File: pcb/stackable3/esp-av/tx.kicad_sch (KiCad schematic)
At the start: 35 parts, among them J6 PJ-327U, J7 PJ-327U, J8 PJ-327U, J9 PJ-327U, Q1 PDNM6ET20V05, Q10 DMP1045U, Q11 DMP1045U, Q12 DMP1045U, Q13 DMP1045U, Q3 DMP1045U, Q4 DMP1045U, Q5 DMP1045U, Q6 DMP1045U

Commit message: Replace discrete resistor footprints with built-ins on stackable3 boards
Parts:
- R18, R19, R20, R22: footprint discrete:R_0603_1608Metric -> Resistor_SMD:R_0603_1608Metric
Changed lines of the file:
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@@
 			)
 		)
-		(property "Footprint" "discrete:R_0603_1608Metric"
+		(property "Footprint" "Resistor_SMD:R_0603_1608Metric"
 			(at 245.11 121.158 90)
 			(effects
@@
 			)
 		)
-		(property "Footprint" "discrete:R_0603_1608Metric"
+		(property "Footprint" "Resistor_SMD:R_0603_1608Metric"
 			(at 245.11 89.408 90)
 			(effects
@@
 			)
 		)
-		(property "Footprint" "discrete:R_0603_1608Metric"
+		(property "Footprint" "Resistor_SMD:R_0603_1608Metric"
 			(at 245.11 152.908 90)
 			(effects
@@
 			)
 		)
-		(property "Footprint" "discrete:R_0603_1608Metric"
+		(property "Footprint" "Resistor_SMD:R_0603_1608Metric"
 			(at 245.11 56.388 90)
 			(effects

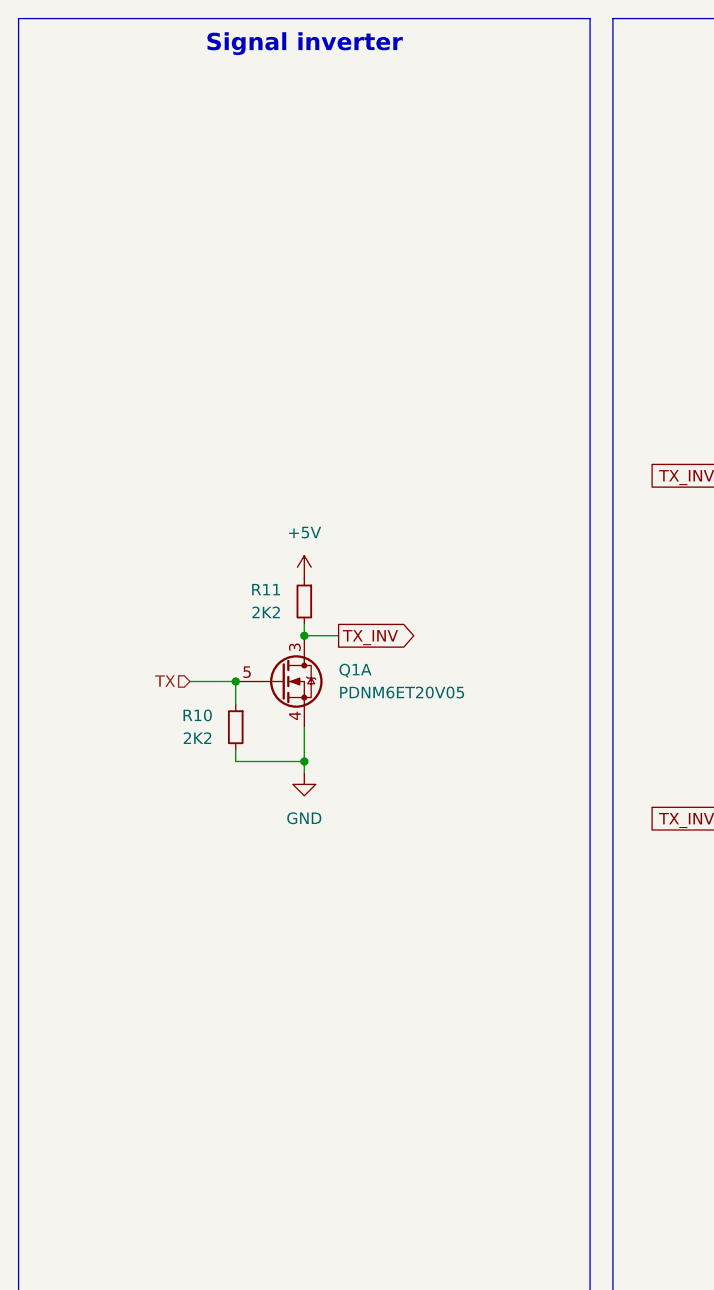
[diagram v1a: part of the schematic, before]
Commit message: Update stackable3/esp-av IR repeater control circuit
This replaces the N-channel repeater signal control MOSFET with a
P-channel MOSFET (driven by an N-channel MOSFET at -5V)
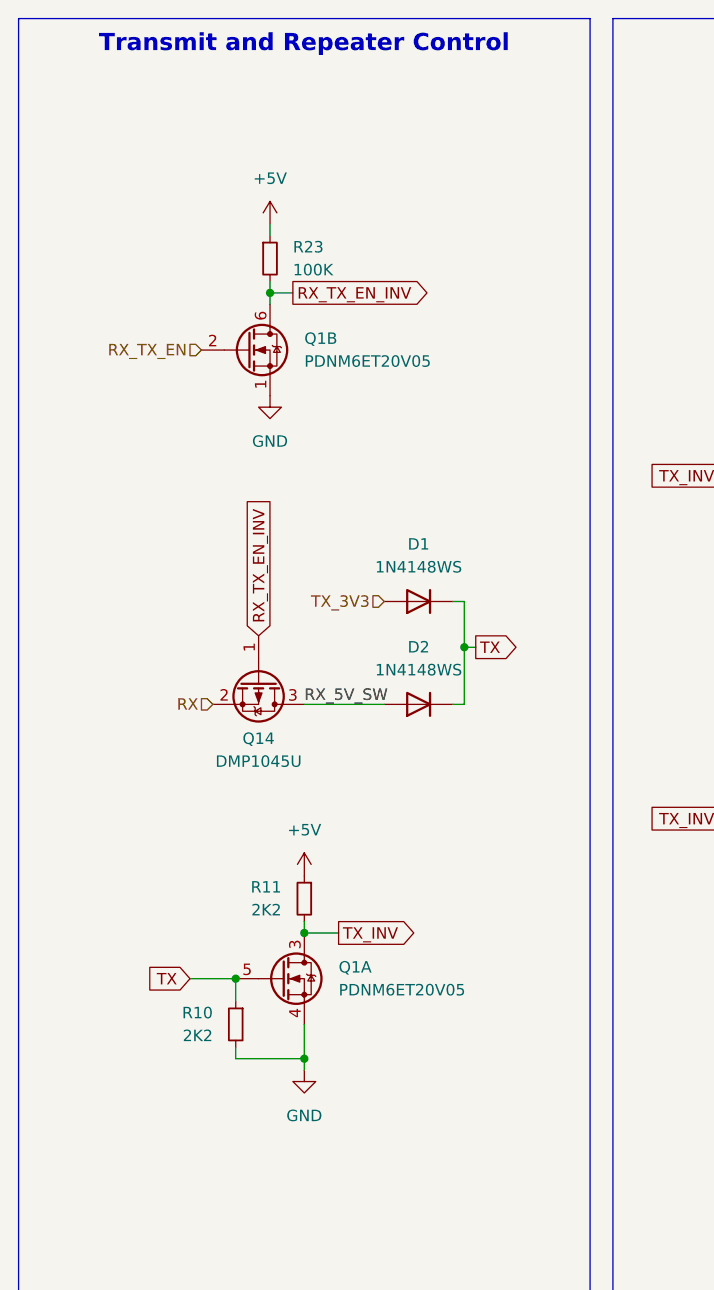
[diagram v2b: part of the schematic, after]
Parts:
- added D1, D2: 1N4148WS, package:D_SOD-323, symbol Diode:1N4148WS
- added unit 2 of Q1
- added Q14: DMP1045U, Package_TO_SOT_SMD:SOT-23, symbol discrete:DMP1045U
- added R23: 100K, Resistor_SMD:R_0603_1608Metric, symbol Device:R_Small
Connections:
- net +5V: now also R23.1
- net GND: now also Q1.1 (S)
- net TX: now also D1.1 (K), D2.1 (K)
- new net RX: Q14.2 (S)
- new net RX_5V_SW: D2.2 (A), Q14.3 (D)
- new net RX_TX_EN: Q1.2 (G)
- new net RX_TX_EN_INV: Q1.6 (D), Q14.1 (G), R23.2
- new net TX_3V3: D1.2 (A)
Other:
- moved on the sheet: Q1A, R10, R11

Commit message: Rename mode LEDs GND net on stackable3/esp-av
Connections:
- net DEBUG_LED_GND renamed MODE_LED_GND
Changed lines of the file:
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@@
 		)
 	)
-	(global_label "DEBUG_LED_GND"
+	(global_label "MODE_LED_GND"
 		(shape output)
 		(at 256.54 54.61 0)
@@
 		)
 	)
-	(global_label "DEBUG_LED_GND"
+	(global_label "MODE_LED_GND"
 		(shape output)
 		(at 256.54 87.63 0)
@@
 		)
 	)
-	(global_label "DEBUG_LED_GND"
+	(global_label "MODE_LED_GND"
 		(shape output)
 		(at 256.54 151.13 0)
@@
 		)
 	)
-	(global_label "DEBUG_LED_GND"
+	(global_label "MODE_LED_GND"
 		(shape output)
 		(at 256.54 119.38 0)

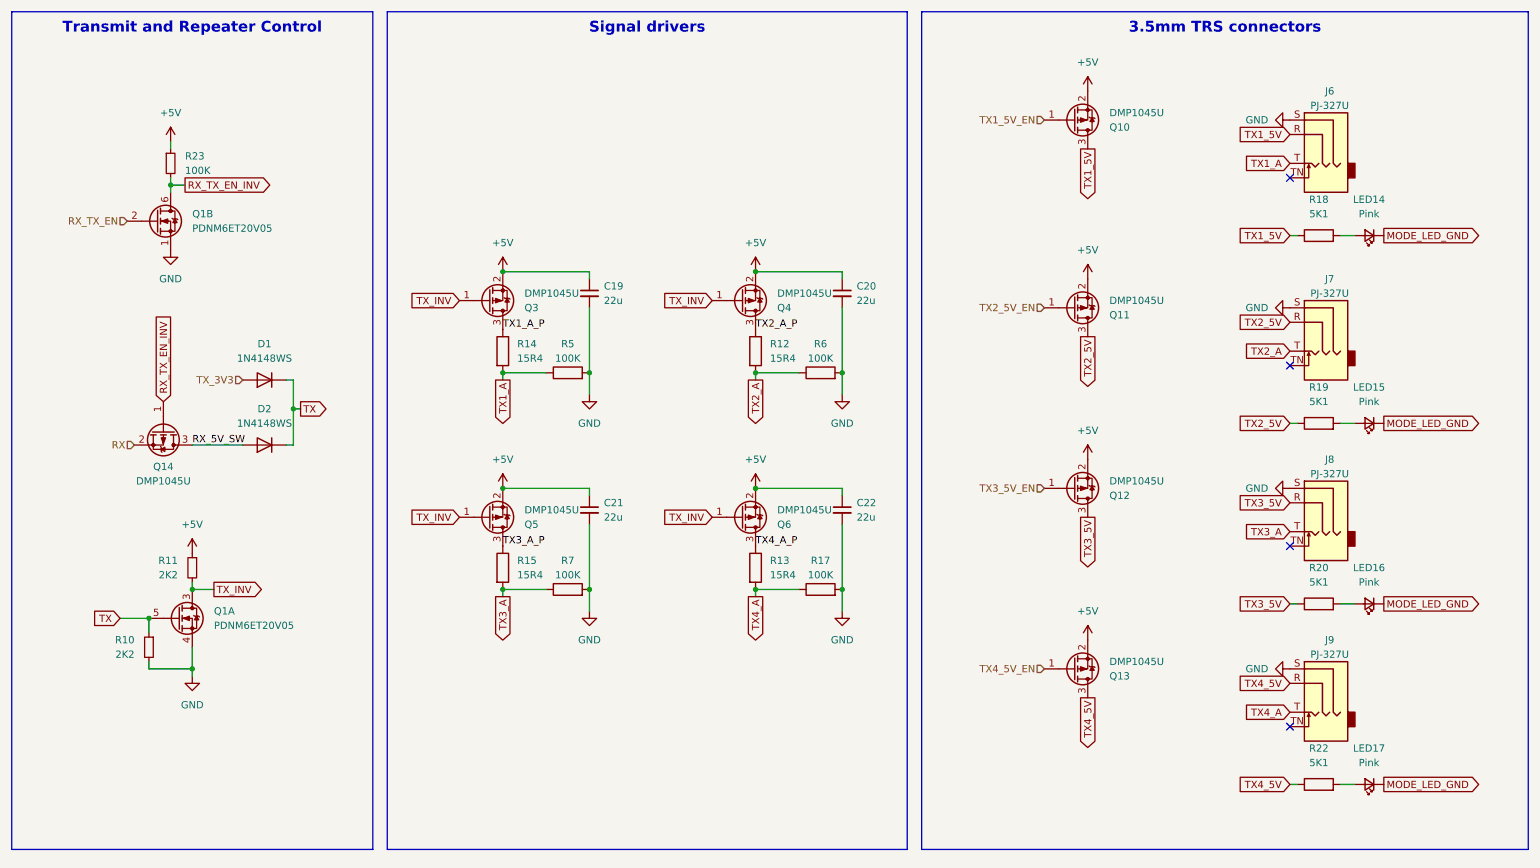
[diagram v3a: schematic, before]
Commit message: Update stackable3/esp-av to v2
Feature changes:
- Add 38kHz RX signal modulation
- Add onboard infrared receiver module (IRM)
- Add JST SH connector for 595 daisy chain outputs
- Add transmit pin socket connector tied to TX1
- Remove neopixel daisy-chain output connectors
- Move indicator LEDs toggle to a 595 output
- Swap RX multiplexer inputs so low select input is non-inverted signal
- Invert repeater enable logic to enable when low
- Add two more mounting holes to PCB

Circuit changes:
- Add power rail short protection on RX connectors
- Add reset IC for 595 start-up state control
- Connect indicator LED MOSFET gate pull-down resistors to ground
- Tie status LED to GND
- Add RX and RX mode pulldown resistors, TX 5V N-channel MOSFET drivers

Component changes:
- Use GT0104SC for logic level translation
- Use 1N5819WT for Schottky diodes
- Use SP2006KT5 P-channel MOSFET for repeater enable
- Use smaller tactile push button for GPIO9/Boot
- Use dual P-channel MOSFETs for TX and TX-5V switches
- Replace aluminum electrolytic capacitors with polymer aluminum
- Replace ME6211C33M5 LDO regulator with DS8242-33SS3
- Change RX/TX indicator LEDs color from blue to green
- Reduce solder paste amount on 0603 SMD LED footprints
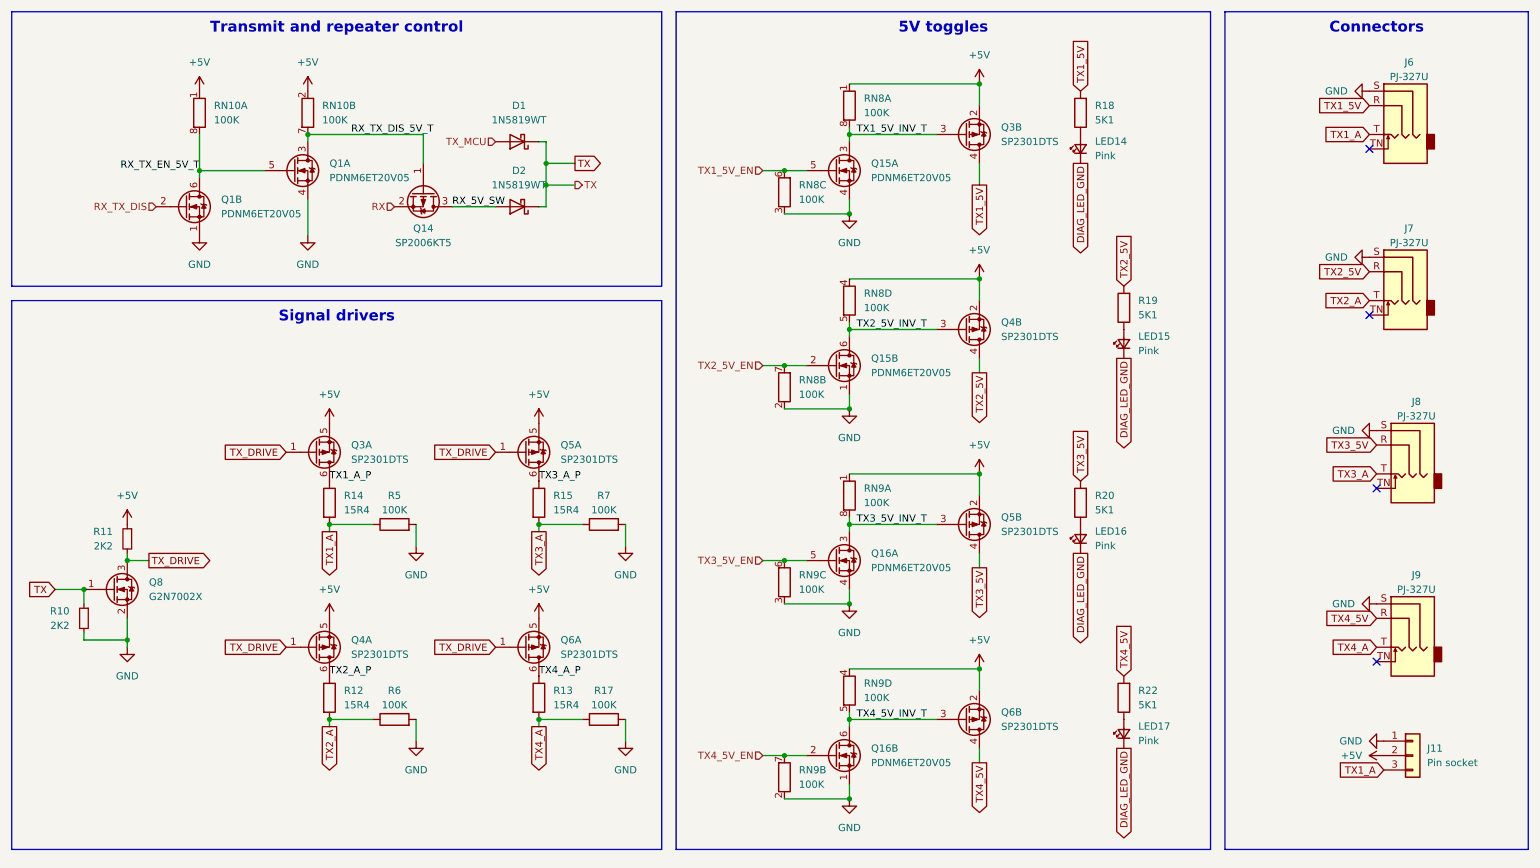
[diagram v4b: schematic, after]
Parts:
- removed C19, C20, C21, C22: 22u, discrete:C_0603_1608Metric, symbol Device:C_Small
- removed D1, D2: 1N4148WS, package:D_SOD-323, symbol Diode:1N4148WS
- removed Q10, Q11, Q12, Q13, Q14, Q3, Q4, Q5, Q6: DMP1045U, Package_TO_SOT_SMD:SOT-23, symbol discrete:DMP1045U
- removed R23: 100K, Resistor_SMD:R_0603_1608Metric, symbol Device:R_Small
- added D1, D2: 1N5819WT, package:D_SOD-523, symbol discrete:1N5819WT
- added J11: Pin socket, Connector_PinSocket_2.54mm:PinSocket_1x03_P2.54mm_Vertical, symbol Connector_Generic:Conn_01x03
- added Q14: SP2006KT5, package:SOT-523, symbol discrete:SP2006KT5
- added Q15, Q16: PDNM6ET20V05, Package_TO_SOT_SMD:SOT-563, symbol discrete:PDNM6ET20V05
- added Q3, Q4, Q5, Q6: SP2301DTS, Package_TO_SOT_SMD:SOT-23-6, symbol discrete:SP2301DTS
- added Q8: G2N7002X, package:SOT-523, symbol discrete:G2N7002X
- added RN10, RN8, RN9: 100K, discrete:R_Array_Convex_4x0603, symbol Device:R_Pack04_Split
- R10, R11: LCSC Part (none) -> C4190
- R17, R5, R6, R7: LCSC Part (none) -> C25803
- R18, R19, R20, R22: LCSC Part (none) -> C23186
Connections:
- net +5V: now also J11.2 (Pin_2), Q3.2 (S2), Q3.5 (S1), Q4.2 (S2), Q4.5 (S1), Q5.2 (S2), Q5.5 (S1), Q6.2 (S2), Q6.5 (S1), RN10.1 (R1.1), RN10.2 (R2.1), RN8.1 (R1.1), RN8.4 (R4.1), RN9.1 (R1.1), RN9.4 (R4.1)
- net GND: now also J11.1 (Pin_1), Q15.1 (S), Q15.4 (S), Q16.1 (S), Q16.4 (S), Q8.2 (S), RN8.2 (R2.1), RN8.3 (R3.1), RN9.2 (R2.1), RN9.3 (R3.1)
- net RX: now also Q14.2 (S)
- net RX_5V_SW: now also D2.2 (A), Q14.3 (D)
- net TX: now also D1.1 (K), D2.1 (K), Q8.1 (G); no longer Q1.5 (G)
- net TX1_5V: now also R18.2, Q3.4 (D2); no longer R18.1
- net TX1_5V_EN: now also Q15.5 (G), RN8.6 (R3.2)
- net TX1_A: now also J11.3 (Pin_3)
- net TX1_A_P: now also Q3.6 (D1)
- net TX2_5V: now also R19.2, Q4.4 (D2); no longer R19.1
- net TX2_5V_EN: now also Q15.2 (G), RN8.7 (R2.2)
- net TX2_A_P: now also Q4.6 (D1)
- net TX3_5V: now also R20.2, Q5.4 (D2); no longer R20.1
- net TX3_5V_EN: now also Q16.5 (G), RN9.6 (R3.2)
- net TX3_A_P: now also Q5.6 (D1)
- net TX4_5V: now also R22.2, Q6.4 (D2); no longer R22.1
- net TX4_5V_EN: now also Q16.2 (G), RN9.7 (R2.2)
- net TX4_A_P: now also Q6.6 (D1)
- net at LED14.2 (A): now also R18.1; no longer R18.2
- net at LED16.2 (A): now also R20.1; no longer R20.2
- net at LED15.2 (A): now also R19.1; no longer R19.2
- net at LED17.2 (A): now also R22.1; no longer R22.2
- net MODE_LED_GND renamed DIAG_LED_GND
- net RX_TX_EN renamed RX_TX_DIS
- net RX_TX_EN_INV renamed RX_TX_EN_5V_T
- net RX_TX_EN_5V_T: now also Q1.5 (G), RN10.8 (R1.2)
- net TX_INV renamed RX_TX_DIS_5V_T
- net RX_TX_DIS_5V_T: now also Q14.1 (G), RN10.7 (R2.2); no longer R11.2
- new net TX1_5V_INV_T: Q15.3 (D), Q3.3 (G2), RN8.8 (R1.2)
- new net TX2_5V_INV_T: Q15.6 (D), Q4.3 (G2), RN8.5 (R4.2)
- new net TX3_5V_INV_T: Q16.3 (D), Q5.3 (G2), RN9.8 (R1.2)
- new net TX4_5V_INV_T: Q16.6 (D), Q6.3 (G2), RN9.5 (R4.2)
- new net TX_DRIVE: Q3.1 (G1), Q4.1 (G1), Q5.1 (G1), Q6.1 (G1), Q8.3 (D), R11.2
- new net TX_MCU: D1.2 (A)
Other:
- moved on the sheet: J6, J7, J8, J9, LED14, LED15, LED16, LED17, Q1A, R10, R11, R12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
